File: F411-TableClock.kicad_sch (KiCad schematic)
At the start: 45 parts, among them J1 USB_C_Receptacle_USB2.0_16P, J2 Conn_01x16_Socket, J3 Conn_01x04_Pin, J4 Conn_01x09_Socket, J5 Conn_01x09_Socket, Q1 DMG3415U, Q2 BC547, SW1 SW_Push, SW2 SW_Push, SW3 SW_Push, SW4 SW_Push, U1 STM32F411CCUx, U2 AP2204K-3.3, U3 AM2302, Y1 Crystal

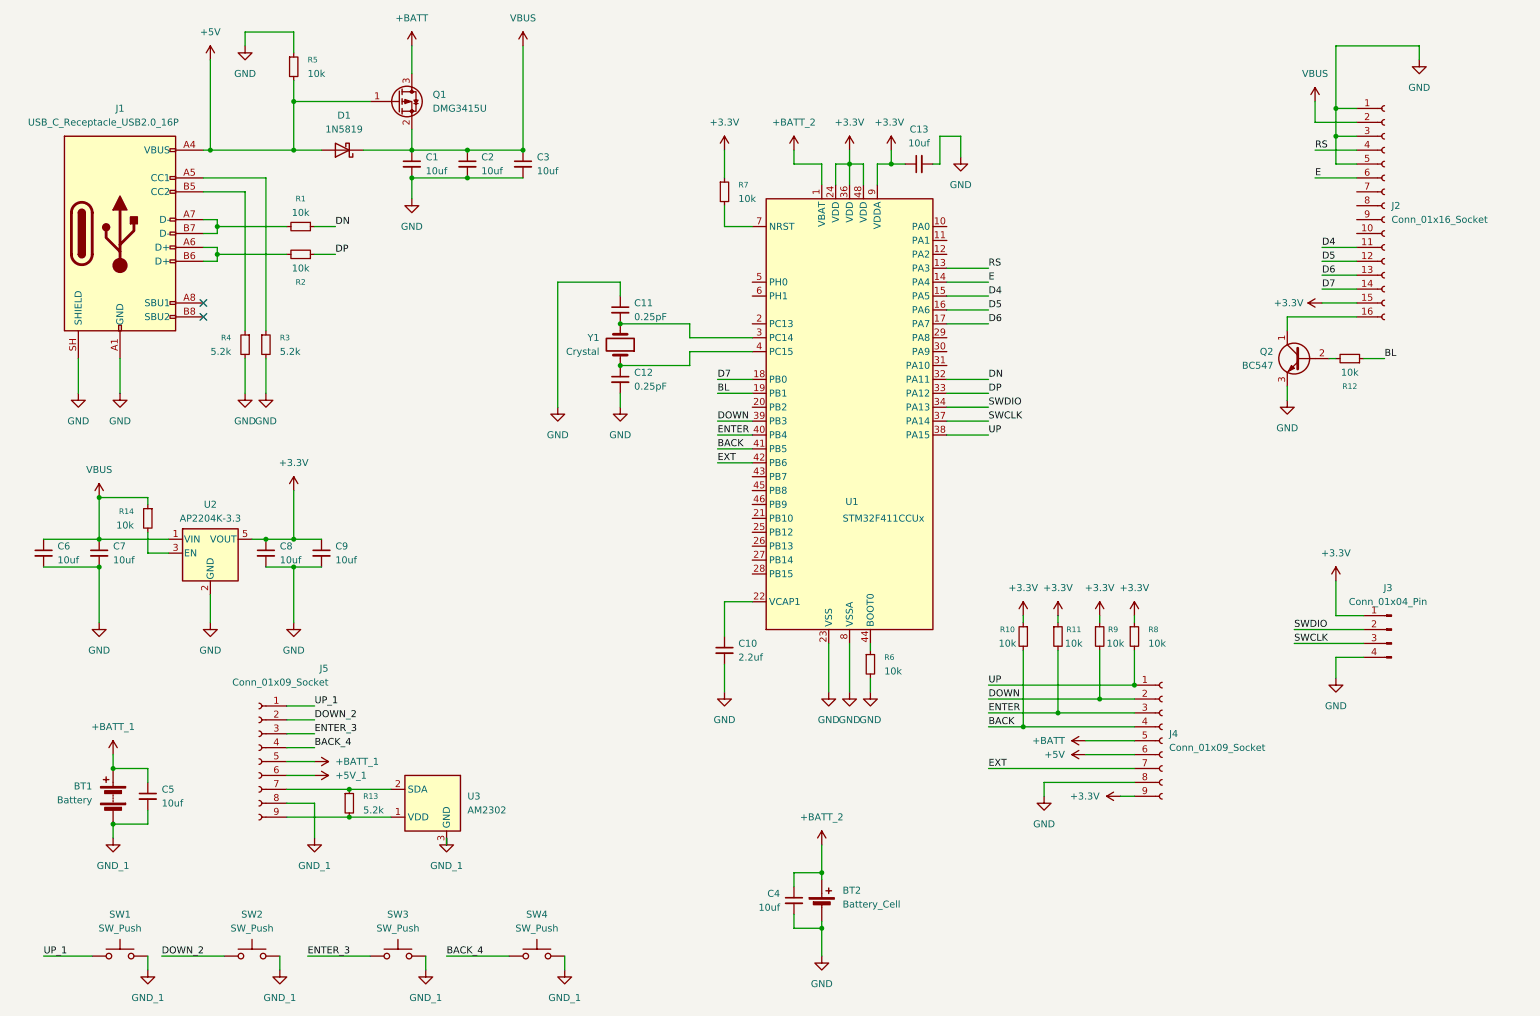
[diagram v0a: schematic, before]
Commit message: Add positions CSV file for component placement in production
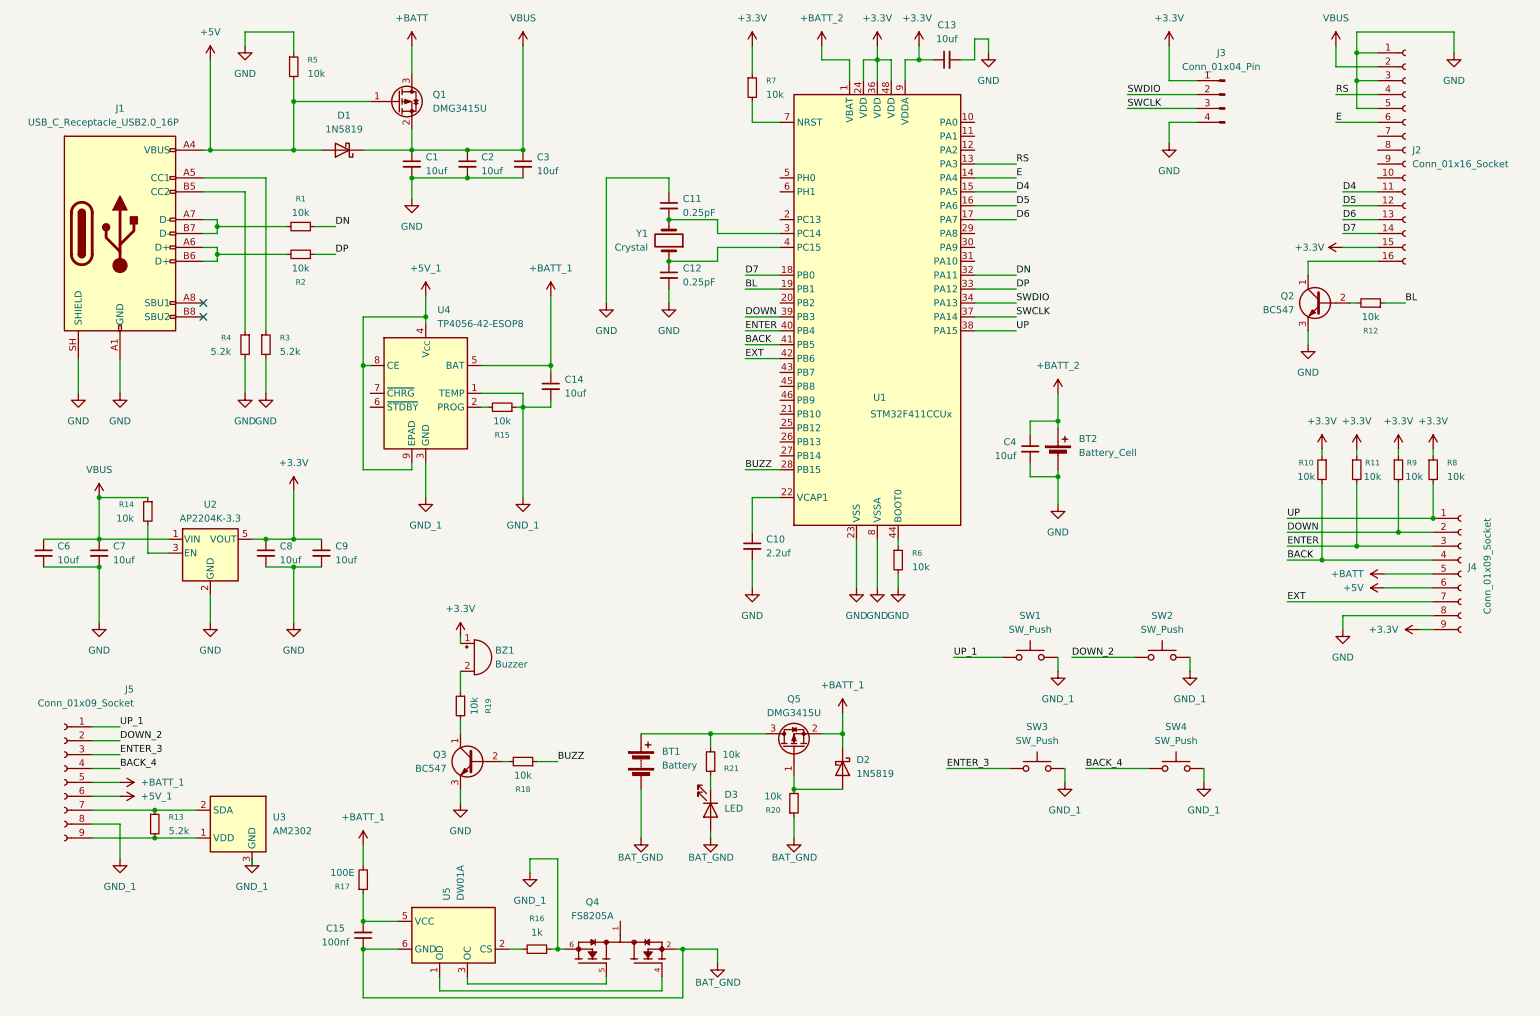
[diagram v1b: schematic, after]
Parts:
- removed C5: 10uf, Capacitor_SMD:C_0805_2012Metric, symbol Device:C_Small
- added BZ1: Buzzer, Buzzer_Beeper:Buzzer_12x9.5RM7.6, symbol Device:Buzzer
- added C14: 10uf, Capacitor_SMD:C_0805_2012Metric, symbol Device:C_Small
- added C15: 100nf, Capacitor_SMD:C_0805_2012Metric, symbol Device:C_Small
- added D2: 1N5819, Diode_SMD:D_0805_2012Metric, symbol Diode:1N5819
- added D3: LED, LED_SMD:LED_0805_2012Metric, symbol Device:LED
- added Q3: BC547, Package_TO_SOT_SMD:TSOT-23, symbol Transistor_BJT:BC547
- added Q4: FS8205A, Package_SO:TSSOP-8_4.4x3mm_P0.65mm, symbol FS8205A:FS8205A
- added Q5: DMG3415U, Package_TO_SOT_SMD:SOT-23, symbol Transistor_FET:DMP3099L
- added R15, R18, R19, R20, R21: 10k, Resistor_SMD:R_0805_2012Metric, symbol Device:R_Small
- added R16: 1k, Resistor_SMD:R_0805_2012Metric, symbol Device:R_Small
- added R17: 100E, Resistor_SMD:R_0805_2012Metric, symbol Device:R_Small
- added U4: TP4056-42-ESOP8, Package_SO:SOIC-8-1EP_3.9x4.9mm_P1.27mm_EP2.41x3.3mm_ThermalVias, symbol Battery_Management:TP4056-42-ESOP8
- added U5: DW01A, Package_TO_SOT_SMD:SOT-23-6, symbol Battery_Management:DW01A
- Q2: footprint Package_TO_SOT_THT:TO-92L_Wide -> Package_TO_SOT_SMD:TSOT-23
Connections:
- net +3.3V: now also BZ1.1 (+)
- net +5V_1: now also U4.4 (V_{CC}), U4.8 (CE), U4.9 (EPAD)
- net +BATT_1: now also C14.1, D2.1 (K), Q5.2 (S), R17.2, U4.5 (BAT); no longer BT1.1 (+)
- net GND: now also Q3.3 (E)
- net GND_1: now also C14.2, Q4.6, Q4.7, R15.1, R16.1, U4.1 (TEMP), U4.3 (GND); no longer BT1.2 (-)
- net BUZZ: now reaches U1.28 (PB15)
- net BUZZ: now also R18.1
- new net: BT1.1 (+), Q5.3 (D), R21.2
- new net: BZ1.2 (-), R19.1
- new net: R15.2, U4.2 (PROG)
- new net: Q3.1 (C), R19.2
- new net: Q3.2 (B), R18.2
- new net: D2.2 (A), Q5.1 (G), R20.2
- new net: C15.2, R17.1, U5.5 (VCC)
- new net: Q4.4, U5.1 (OD)
- new net: R16.2, U5.2 (CS)
- new net: Q4.5, U5.3 (OC)
- new net: D3.1 (K), R21.1
- new net: Q4.1, Q4.8
- new net BAT_GND: BT1.2 (-), C15.1, D3.2 (A), Q4.2, Q4.3, R20.1, U5.6 (GND)
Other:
- moved on the sheet: BT1, BT2, C10, C11, C12, C13, C4, J2, J3, J4, J5, Q2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
